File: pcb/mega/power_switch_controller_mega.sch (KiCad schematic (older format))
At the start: 58 parts, among them P1 PWR_JACK_2.5x5.5, P10 HEADER_02X08_SMD, P11 HEADER_02X08_SMD, P2 HEADER_01X03_SMD_RA, P3 HEADER_01X03_SMD_RA, P4 HEADER_01X03_SMD_RA, P5 HEADER_01X03_SMD_RA, P6 HEADER_01X02_SMD_RA, P7 BNC_DOUBLE_RA, P8 HEADER_02X08_SMD, P9 HEADER_02X08_SMD, SW1 SPST_SLIDE_AS, U1 TLE7230R, U2 TLE7230R, U3 TLE7230R, U4 TLE7230R

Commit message: Create mega pcb.
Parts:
- ARDUINO1: footprint power_switch_controller:ARDUINO_MEGA_SHIELD -> power_switch_controller_mega:ARDUINO_MEGA_SHIELD
- C1, C2, C3, C4, C5, C6, C7: footprint power_switch_controller:SM1210 -> power_switch_controller_mega:SM1210
- D1, D10, D11, D12, D13, D14, D15, D16, D17, D18, D19, D2, D20, D21, D22, D23, D24, D25, D26, D27, D28, D29, D3, D30, D31, D32, D33, D4, D5, D6, D7, D8, D9: footprint power_switch_controller:LED_555-3XXX -> power_switch_controller_mega:LED_555-3XXX
- P1: footprint power_switch_controller:DCJACK_2PIN_HIGHCURRENT -> power_switch_controller_mega:DCJACK_2PIN_HIGHCURRENT
- P10, P11, P8, P9: footprint power_switch_controller:HEADER_02x08_SMD -> power_switch_controller_mega:HEADER_02x08_SMD; Description CONN HEADER LO-PRO 16POS AU SMD -> CONN HEADR 2.54MM 16POS GOLD SMD; PartNumber HSL16H-ND -> S9187-ND
- P2, P3, P4, P5: footprint power_switch_controller:Header_3_Pin_SMD_RA -> power_switch_controller_mega:Header_3_Pin_SMD_RA
- P6: footprint power_switch_controller:Header_2_Pin_SMD_RA -> power_switch_controller_mega:Header_2_Pin_SMD_RA
- P7: footprint power_switch_controller:BNC_DOUBLE -> power_switch_controller_mega:BNC_DOUBLE
- REG1: footprint power_switch_controller:DC_DC_CONV_R78C -> power_switch_controller_mega:DC_DC_CONV_R78C
- SW1: footprint power_switch_controller:SPST_SLIDE_AS -> power_switch_controller_mega:SPST_SLIDE_AS
- U1, U2, U3, U4: footprint power_switch_controller:PG-DSO-36 -> power_switch_controller_mega:PG-DSO-36

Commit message: Progress towards mega pcb 1.6.
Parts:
- removed REG1: CONV_DC_DC_12V_1A, power_switch_controller_mega:DC_DC_CONV_R78C, symbol CONV_DC_DC_12V_1A
- added D1: diode_schottky_45V_10A, power_switch_controller_mega:CFP15, symbol diode_schottky_45V_10A
- added REG1: CONV_DC_DC_9V_1A, power_switch_controller_mega:DC_DC_CONV_R78C, symbol CONV_DC_DC_9V_1A
- renumbered D1 to L1, D10 to L10, D11 to L11, D12 to L12, D13 to L13, D14 to L14, D15 to L15, D16 to L16, D17 to L17, D18 to L18, D19 to L19, D2 to L2, D20 to L20, D21 to L21, D22 to L22, D23 to L23, D24 to L24, D25 to L25, D26 to L26, D27 to L27, D28 to L28, D29 to L29, D3 to L3, D30 to L30, D31 to L31, D32 to L32, D33 to L33, D4 to L4, D5 to L5, D6 to L6, D7 to L7, D8 to L8, D9 to L9
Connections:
- net +5V: now also U1.12 (IN3), U1.6 (IN1), U1.7 (IN2), U2.12 (IN3), U2.6 (IN1), U2.7 (IN2), U3.12 (IN3), U3.6 (IN1), U3.7 (IN2), U4.12 (IN3), U4.6 (IN1), U4.7 (IN2)
- net GND: now also REG1.2 (GND); no longer U1.12 (IN3), U1.13 (IN4), U1.6 (IN1), U1.7 (IN2), U2.12 (IN3), U2.13 (IN4), U2.6 (IN1), U2.7 (IN2), U3.12 (IN3), U3.13 (IN4), U3.6 (IN1), U3.7 (IN2), U4.12 (IN3), U4.13 (IN4), U4.6 (IN1), U4.7 (IN2)
- net VAA: now also D1.2 (A), REG1.1 (+VIN); no longer P6.2 (P2)
- net V_IN: now also REG1.3 (+VOUT)
- net IN: now reaches ARDUINO1.45 (D45/PWM/OC5B/PL4)
- net IN: now also U1.13 (IN4), U2.13 (IN4), U3.13 (IN4), U4.13 (IN4)
- new net VCC: D1.1 (K), P6.2 (P2)
- no-connect marks 73 -> 72
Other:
- moved on the sheet: C2, C3, C4, C5, C6, C7

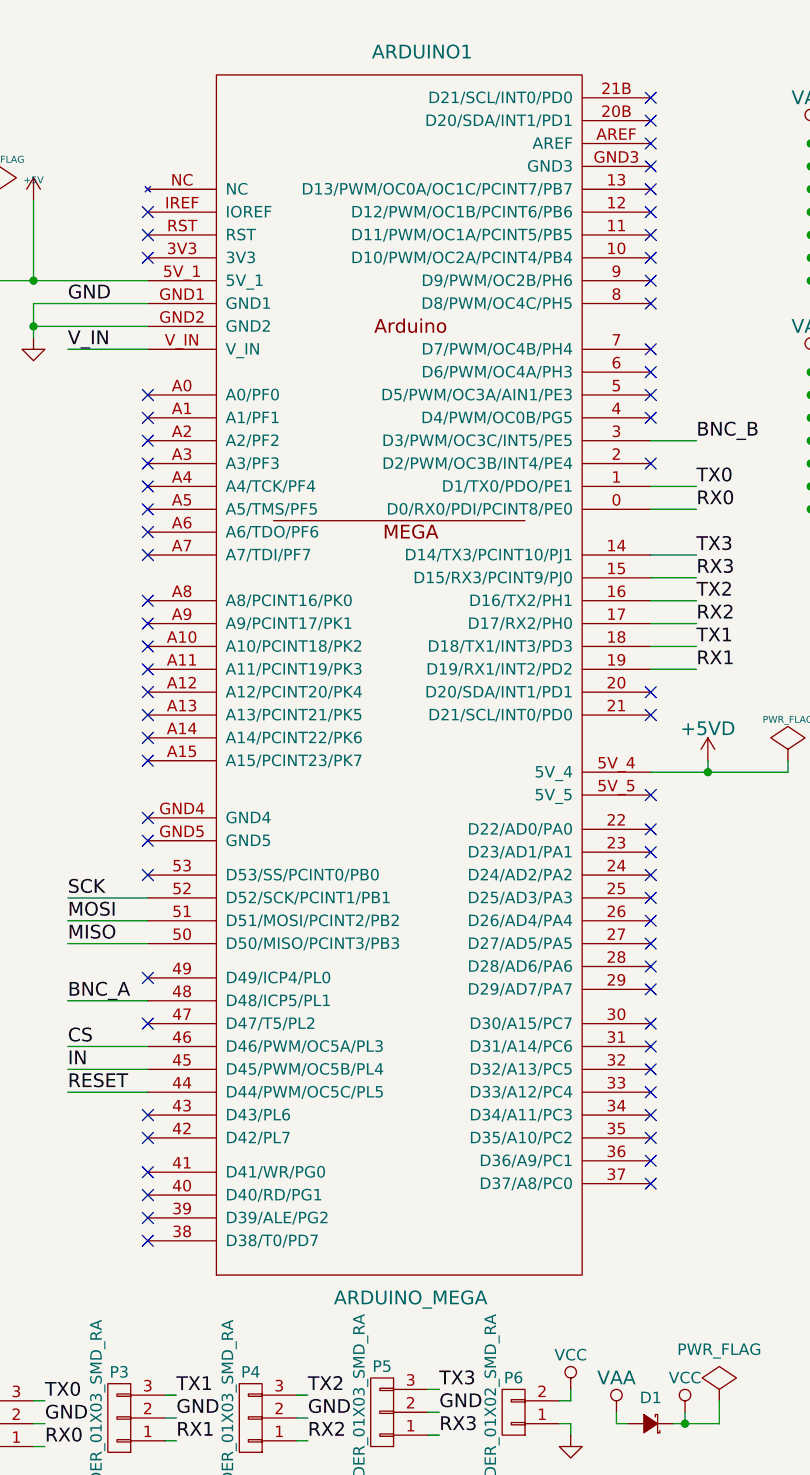
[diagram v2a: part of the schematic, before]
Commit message: Updated Arduino Mega digikey part number.
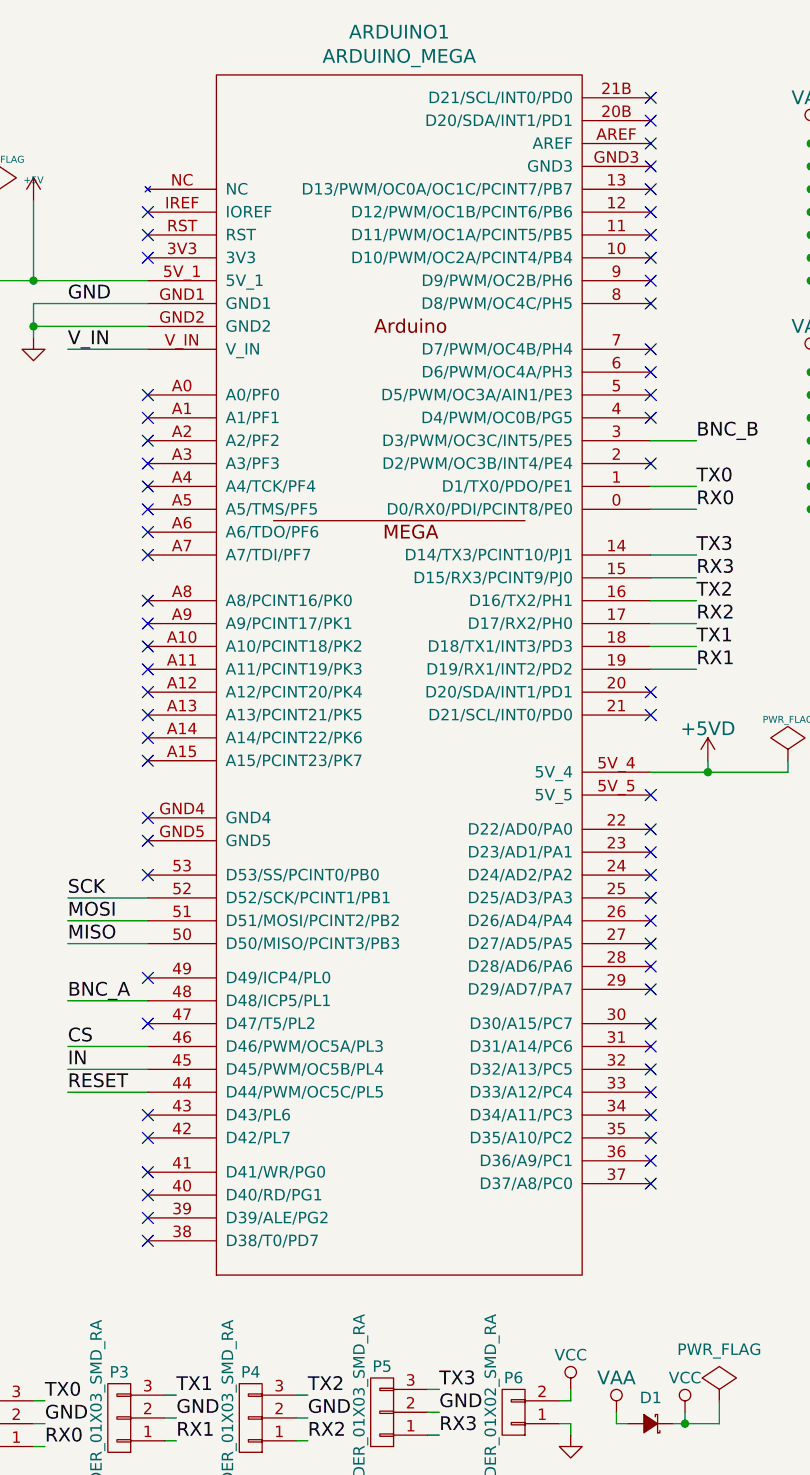
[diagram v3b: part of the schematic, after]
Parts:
- ARDUINO1: Description BOARD MCU MEGA2560 -> ARDUINO MEGA 2560; PartNumber 1050-1018-ND -> 1659-1001-ND
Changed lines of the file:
@@
 OUT15
-$Comp
-L ARDUINO_MEGA ARDUINO1
-U 1 1 54AD3990
-P 2500 3350
-F 0 "ARDUINO1" H 2550 6100 60  0000 C CNN
-F 1 "ARDUINO_MEGA" H 2500 650 60  0000 C CNN
-F 2 "power_switch_controller_mega:ARDUINO_MEGA_SHIELD" H 2450 6000 60  0001 C CNN
-F 3 "" H 2550 6100 60  0000 C CNN
-F 4 "digikey" H 2650 6200 60  0001 C CNN "Vendor"
-F 5 "1050-1018-ND" H 2750 6300 60  0001 C CNN "PartNumber"
-F 6 "BOARD MCU MEGA2560" H 2850 6400 60  0001 C CNN "Description"
-	1    2500 3350
-	1    0    0    -1
-$EndComp
 $Comp
 L GND #PWR016
@@
 Text Label 4350 7250 0    60   ~ 0
 V_IN
+$Comp
+L ARDUINO_MEGA ARDUINO1
+U 1 1 576C0AF4
+P 2500 3350
+F 0 "ARDUINO1" H 2450 6187 60  0000 C CNN
+F 1 "ARDUINO_MEGA" H 2450 6081 60  0000 C CNN
+F 2 "power_switch_controller_mega:ARDUINO_MEGA_SHIELD" H 2450 6000 60  0001 C CNN
+F 3 "" H 2550 6100 60  0000 C CNN
+F 4 "digikey" H 2650 6200 60  0001 C CNN "Vendor"
+F 5 "1659-1001-ND" H 2750 6300 60  0001 C CNN "PartNumber"
+F 6 "ARDUINO MEGA 2560" H 2850 6400 60  0001 C CNN "Description"
+	1    2500 3350
+	1    0    0    -1
+$EndComp
 $EndSCHEMATC

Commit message: Progess towards mega pcb1.7.
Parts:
- added C8: 0.1uF, power_switch_controller_mega:SM1210, symbol 0.1uF
- added R1, R2: 10.0k, power_switch_controller_mega:SM1210, symbol 10.0k
- added U5: PCA9685, power_switch_controller_mega:TSSOP28, symbol PCA9685
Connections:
- net +5V: now also C8.1, R1.1, R2.1, U5.28 (VDD)
- net GND: now also C8.2, U5.1 (A0), U5.14 (GND), U5.2 (A1), U5.24 (A5), U5.25 (EXTCLK), U5.3 (A2), U5.4 (A3), U5.5 (A4)
- net SDA: now reaches ARDUINO1.20B (D20/SDA/INT1/PD1)
- net SDA: now also R1.2, U5.27 (SDA)
- net SCL: now reaches ARDUINO1.21B (D21/SCL/INT0/PD0)
- net SCL: now also R2.2, U5.26 (SCL)
- removed net IN: ARDUINO1.45 (D45/PWM/OC5B/PL4), U1.13 (IN4), U2.13 (IN4), U3.13 (IN4), U4.13 (IN4)
- new net ENABLE: ARDUINO1.45 (D45/PWM/OC5B/PL4), U5.23 (~ENABLE)
- new net PWM0: U1.13 (IN4), U5.6 (PWM0)
- new net PWM1: U2.13 (IN4), U5.7 (PWM1)
- new net PWM2: U3.13 (IN4), U5.8 (PWM2)
- new net PWM3: U4.13 (IN4), U5.9 (PWM3)
- no-connect marks 72 -> 82
